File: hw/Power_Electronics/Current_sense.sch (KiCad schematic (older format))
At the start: 45 parts, among them U3 TSV912IDT, U4 TSV912IDT

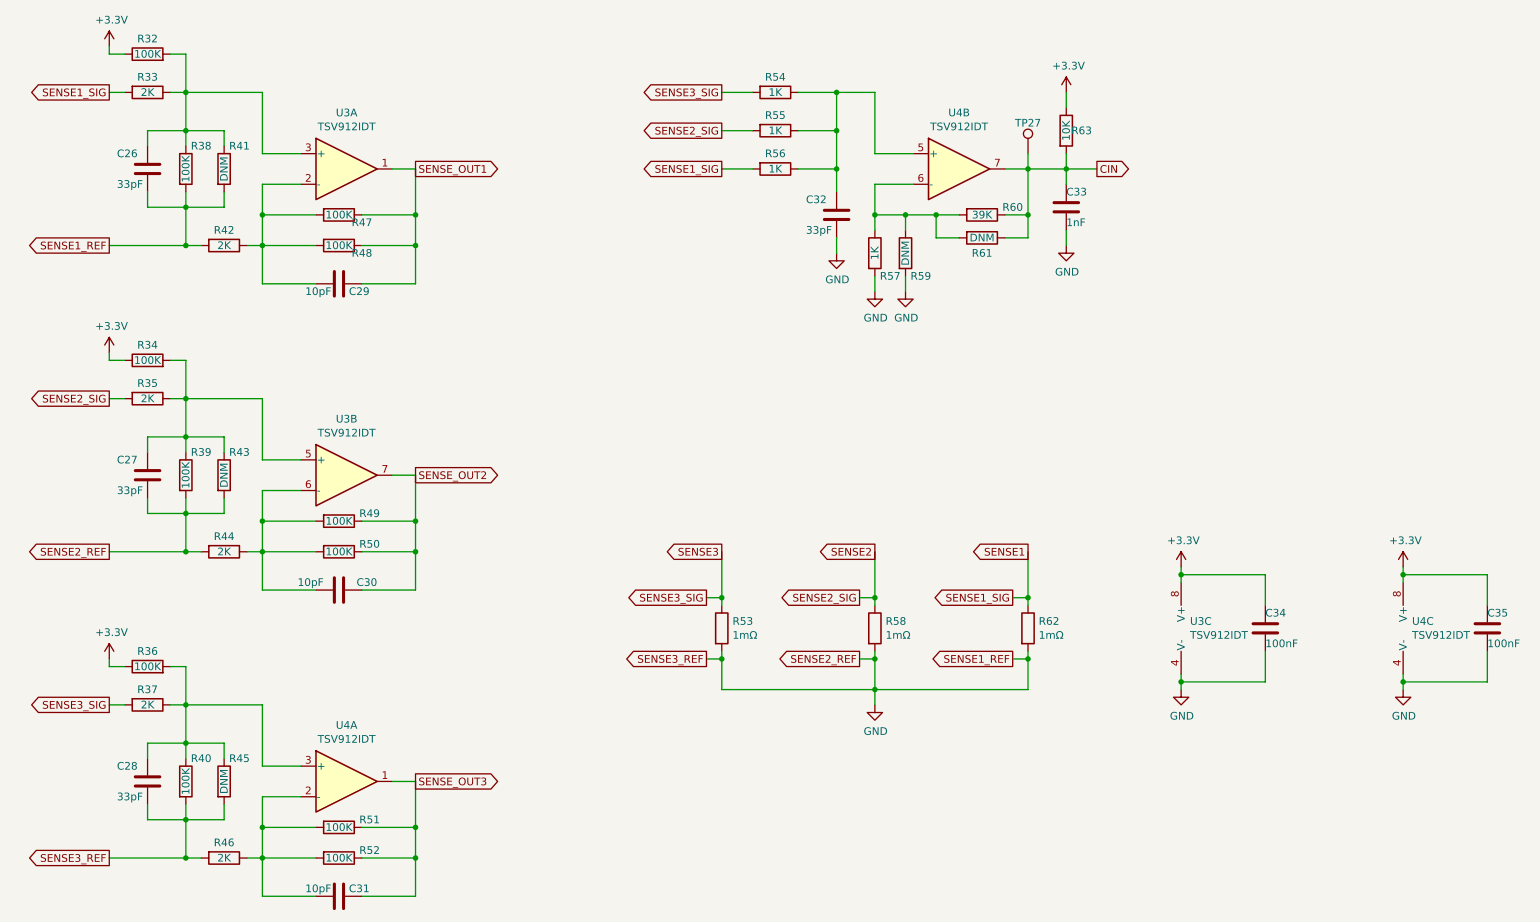
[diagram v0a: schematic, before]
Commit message: update schematic with hall and BEMF circuits
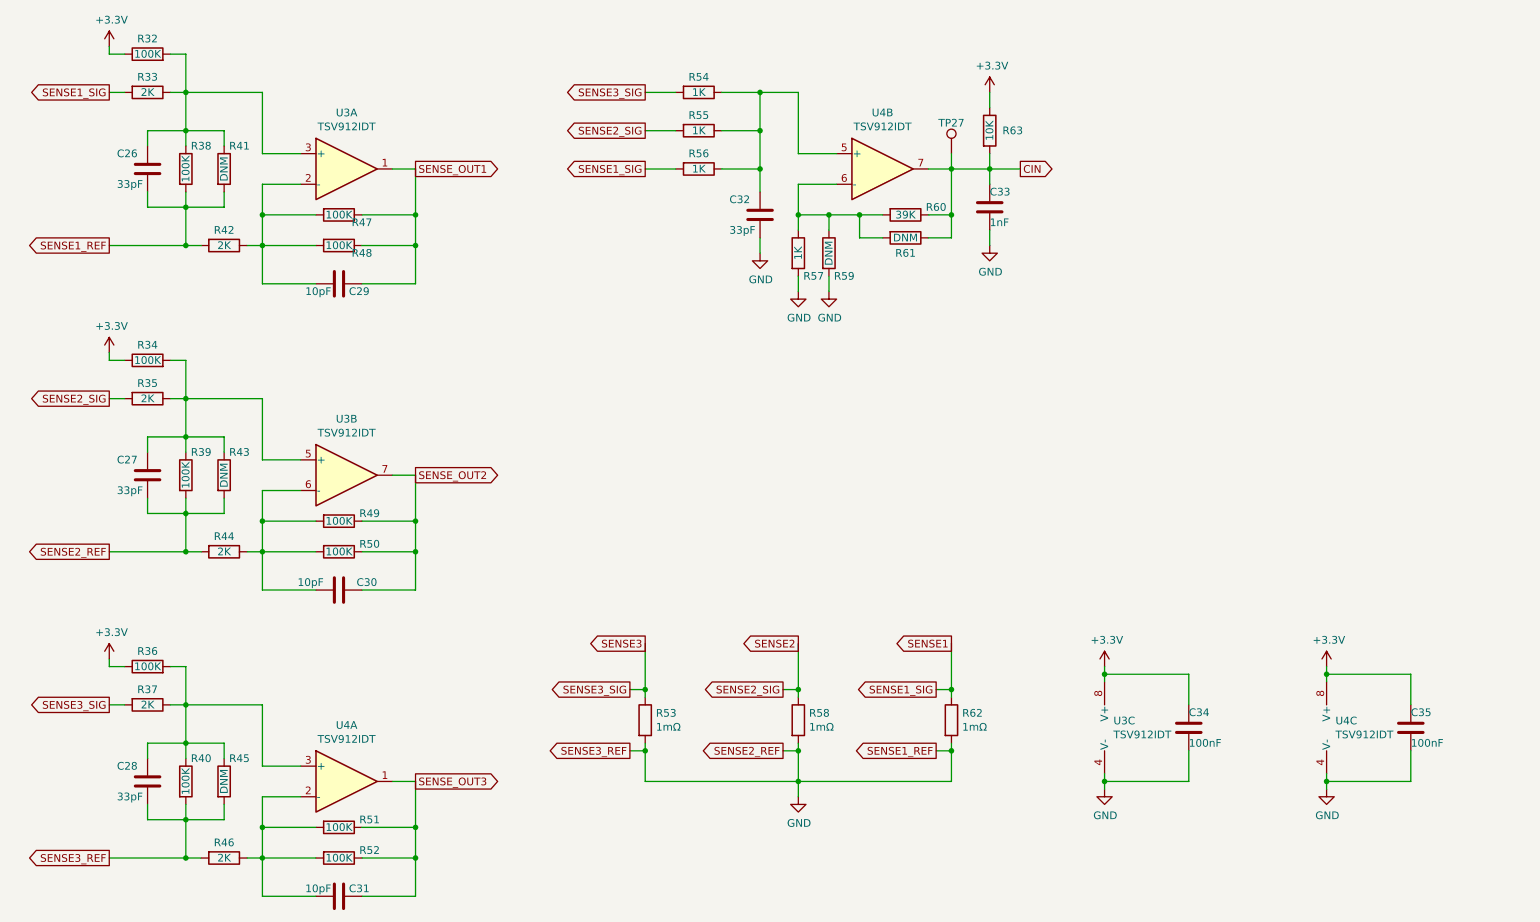
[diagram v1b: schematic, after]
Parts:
- R63: LCSC (none) -> C25804
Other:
- moved on the sheet: C32, C33, C34, C35, R53, R54, R55, R56, R57, R58, R59, R60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

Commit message: all component's positions are more or less defined
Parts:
- renumbered C26 to C32, C27 to C33, C28 to C34, C29 to C35, C30 to C36, C31 to C37, C32 to C38, C33 to C39, C34 to C40, C35 to C41, R32 to R53, R33 to R54, R34 to R55, R35 to R56, R36 to R57, R37 to R58, R38 to R59, R39 to R60, R40 to R61, R41 to R62, R42 to R63, R43 to R64, R44 to R65, R45 to R66, R46 to R67, R47 to R68, R48 to R69, R49 to R70, R50 to R71, R51 to R72, R52 to R73, R53 to R74, R54 to R75, R55 to R76, R56 to R77, R57 to R78, R58 to R79, R59 to R80, R60 to R81, R61 to R82, R62 to R83, R63 to R84, TP27 to TP30

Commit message: adjustments made on silkscreen layer
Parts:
- removed R74, R79, R83: 1mΩ, inversor-pmsm:R_2512_6332Metric, symbol Device:R
- added R82, R87, R91: 1mΩ, inversor-pmsm:R_2512_6332Metric, symbol Device:R_Shunt
- renumbered C32 to C35, C33 to C36, C34 to C37, C35 to C38, C36 to C39, C37 to C40, C38 to C41, C39 to C42, C40 to C43, C41 to C44, R53 to R61, R54 to R62, R55 to R63, R56 to R64, R57 to R65, R58 to R66, R59 to R67, R60 to R68, R61 to R69, R62 to R70, R63 to R71, R64 to R72, R65 to R73, R66 to R74, R67 to R75, R68 to R76, R69 to R77, R70 to R78, R71 to R79, R72 to R80, R73 to R81, R75 to R83, R76 to R84, R77 to R85, R78 to R86, R80 to R88, R81 to R89, R82 to R90, R84 to R92, TP30 to TP40
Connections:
- net GND: now also R82.1, R87.1, R91.1; no longer C35.2, C36.2, C37.2, R67.2, R68.2, R69.2, R70.2, R71.2, R72.2, R73.2, R74.2, R75.2
- net SENSE1: now also R91.4; no longer R62.2, R85.2
- net SENSE2: now also R87.4; no longer R64.2, R84.2
- net SENSE3: now also R82.4; no longer R66.2, R83.2
- new net SENSE1_REF: C35.2, R67.2, R70.2, R71.2, R91.2
- new net SENSE1_SIG: R62.2, R85.2, R91.3
- new net SENSE2_REF: C36.2, R68.2, R72.2, R73.2, R87.2
- new net SENSE2_SIG: R64.2, R84.2, R87.3
- new net SENSE3_REF: C37.2, R69.2, R74.2, R75.2, R82.2
- new net SENSE3_SIG: R66.2, R82.3, R83.2

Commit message: adjusts made on mask layer to expose high current path
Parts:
- removed TP40: TestPoint, TestPoint:TestPoint_Pad_D1.5mm, symbol Connector:TestPoint
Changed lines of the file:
@@
 Wire Wire Line
 	6400 2300 6200 2300
-$Comp
-L Connector:TestPoint TP?
-U 1 1 606A739D
-P 7000 1900
-AR Path="/606A739D" Ref="TP?"  Part="1"
-AR Path="/6016C275/606A739D" Ref="TP40"  Part="1"
-F 0 "TP40" H 7000 2100 50  0000 C CNN
-F 1 "TestPoint" H 7058 1927 50  0001 L CNN
-F 2 "TestPoint:TestPoint_Pad_D1.5mm" H 7200 1900 50  0001 C CNN
-F 3 "~" H 7200 1900 50  0001 C CNN
-	1    7000 1900
-	1    0    0    -1
-$EndComp
 Connection ~ 7000 2000
-Wire Wire Line
-	7000 2000 7000 1900
 $Comp
 L Device:R R?

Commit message: create high voltage net class and solve DRC erros
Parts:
- C35, C36, C37, C41: value 33pF -> 12pF; LCSC C1663 -> C38523
- C38, C39, C40: value 10pF -> 12pF; LCSC C1634 -> C38523
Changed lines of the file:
@@
 AR Path="/6016C275/6021EF15" Ref="C36"  Part="1"
 F 0 "C36" H 1550 4100 50  0000 L CNN
-F 1 "33pF" H 1550 3900 50  0000 L CNN
+F 1 "12pF" H 1550 3900 50  0000 L CNN
 F 2 "Capacitor_SMD:C_0603_1608Metric" H 1788 3850 50  0001 C CNN
 F 3 "Samsung-Electro-Mechanics-CL10C330JB8NNNC_C1663.pdf" H 1750 4000 50  0001 C CNN
-F 4 "C1663" H 1750 4000 50  0001 C CNN "LCSC"
+F 4 "C38523" H 1750 4000 50  0001 C CNN "LCSC"
 	1    1750 4000
 	1    0    0    -1
@@
 AR Path="/6016C275/6021EF78" Ref="C39"  Part="1"
 F 0 "C39" V 3050 4500 50  0000 L CNN
-F 1 "10pF" V 3050 4850 50  0000 L CNN
+F 1 "12pF" V 3050 4850 50  0000 L CNN
 F 2 "Capacitor_SMD:C_0603_1608Metric" H 3038 4600 50  0001 C CNN
 F 3 "Samsung-Electro-Mechanics-CL10C330JB8NNNC_C1663.pdf" H 3000 4750 50  0001 C CNN
-F 4 "C1634" H 3000 4750 50  0001 C CNN "LCSC"
+F 4 "C38523" H 3000 4750 50  0001 C CNN "LCSC"
 	1    3000 4750
 	0    -1   -1   0
@@
 AR Path="/6016C275/60286010" Ref="C35"  Part="1"
 F 0 "C35" H 1550 2100 50  0000 L CNN
-F 1 "33pF" H 1550 1900 50  0000 L CNN
+F 1 "12pF" H 1550 1900 50  0000 L CNN
 F 2 "Capacitor_SMD:C_0603_1608Metric" H 1788 1850 50  0001 C CNN
 F 3 "Samsung-Electro-Mechanics-CL10C330JB8NNNC_C1663.pdf" H 1750 2000 50  0001 C CNN
-F 4 "C1663" H 1750 2000 50  0001 C CNN "LCSC"
+F 4 "C38523" H 1750 2000 50  0001 C CNN "LCSC"
 	1    1750 2000
 	1    0    0    -1
@@
 AR Path="/6016C275/60286089" Ref="C38"  Part="1"
 F 0 "C38" V 2950 2550 50  0000 L CNN
-F 1 "10pF" V 2950 2800 50  0000 L CNN
+F 1 "12pF" V 2950 2800 50  0000 L CNN
 F 2 "Capacitor_SMD:C_0603_1608Metric" H 3038 2600 50  0001 C CNN
 F 3 "Samsung-Electro-Mechanics-CL10C330JB8NNNC_C1663.pdf" H 3000 2750 50  0001 C CNN
-F 4 "C1634" H 3000 2750 50  0001 C CNN "LCSC"
+F 4 "C38523" H 3000 2750 50  0001 C CNN "LCSC"
 	1    3000 2750
 	0    -1   -1   0
@@
 AR Path="/6016C275/6028F1BC" Ref="C37"  Part="1"
 F 0 "C37" H 1550 6100 50  0000 L CNN
-F 1 "33pF" H 1550 5900 50  0000 L CNN
+F 1 "12pF" H 1550 5900 50  0000 L CNN
 F 2 "Capacitor_SMD:C_0603_1608Metric" H 1788 5850 50  0001 C CNN
 F 3 "Samsung-Electro-Mechanics-CL10C330JB8NNNC_C1663.pdf" H 1750 6000 50  0001 C CNN
-F 4 "C1663" H 1750 6000 50  0001 C CNN "LCSC"
+F 4 "C38523" H 1750 6000 50  0001 C CNN "LCSC"
 	1    1750 6000
 	1    0    0    -1
@@
 AR Path="/6016C275/6028F235" Ref="C40"  Part="1"
 F 0 "C40" V 3050 6550 50  0000 L CNN
-F 1 "10pF" V 3050 6800 50  0000 L CNN
+F 1 "12pF" V 3050 6800 50  0000 L CNN
 F 2 "Capacitor_SMD:C_0603_1608Metric" H 3038 6600 50  0001 C CNN
 F 3 "Samsung-Electro-Mechanics-CL10C330JB8NNNC_C1663.pdf" H 3000 6750 50  0001 C CNN
-F 4 "C1634" H 3000 6750 50  0001 C CNN "LCSC"
+F 4 "C38523" H 3000 6750 50  0001 C CNN "LCSC"
 	1    3000 6750
 	0    -1   -1   0
@@
 AR Path="/6016C275/6060925A" Ref="C41"  Part="1"
 F 0 "C41" H 5550 2400 50  0000 L CNN
-F 1 "33pF" H 5550 2200 50  0000 L CNN
+F 1 "12pF" H 5550 2200 50  0000 L CNN
 F 2 "Capacitor_SMD:C_0603_1608Metric" H 5788 2150 50  0001 C CNN
 F 3 "Samsung-Electro-Mechanics-CL10C330JB8NNNC_C1663.pdf" H 5750 2300 50  0001 C CNN
-F 4 "C1663" H 5750 2300 50  0001 C CNN "LCSC"
+F 4 "C38523" H 5750 2300 50  0001 C CNN "LCSC"
 	1    5750 2300
 	1    0    0    -1
